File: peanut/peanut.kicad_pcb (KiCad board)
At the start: 4 copper layers, 48.2 x 24.5 mm, 75 parts, among them J1 USB-C, J2 PYRO_OUT, J3 Battery JST, J4 Arming, Q1 NMOS, Q2 NMOS, Q3 NMOS, Q4 NMOS, Q5 PMOS, U1 MS5611-01BA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

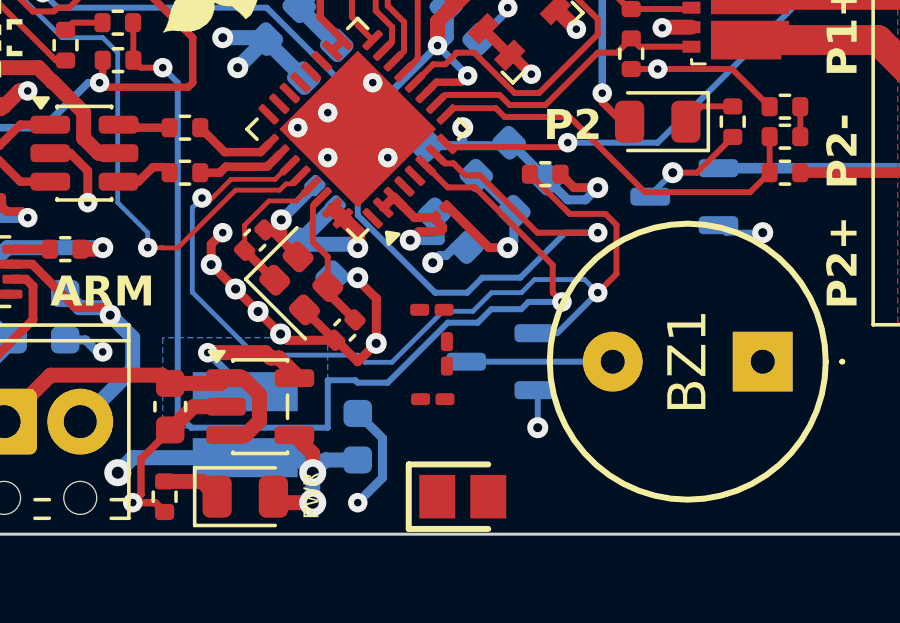
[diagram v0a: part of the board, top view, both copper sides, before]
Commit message: feat: Route the Bluetooth trace
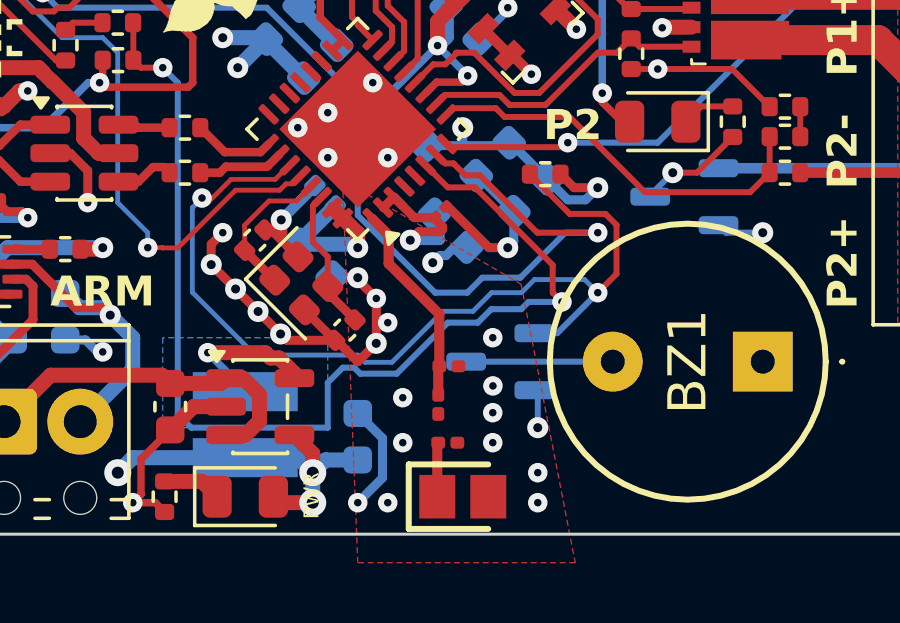
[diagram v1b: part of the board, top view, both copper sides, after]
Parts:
- C12, C13: footprint Capacitor_SMD:C_0201_0603Metric_Pad0.64x0.40mm_HandSolder -> Capacitor_SMD:C_0201_0603Metric
- L2: footprint Inductor_SMD:L_0201_0603Metric_Pad0.64x0.40mm_HandSolder -> Inductor_SMD:L_0201_0603Metric
- moved C12 1.97 mm to (146.0, 103.9), turned to 0 degrees
- moved L2 1.71 mm to (145.7, 105.2)
- moved C13 1.53 mm to (146.0, 106.4), turned to 0 degrees
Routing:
- net /RF_LNA_IN: track 0.00 -> 6.81 mm
- net /RF: track 0.00 -> 1.88 mm
- net GND: vias 38 -> 49
- added copper zone on F.Cu, net GND

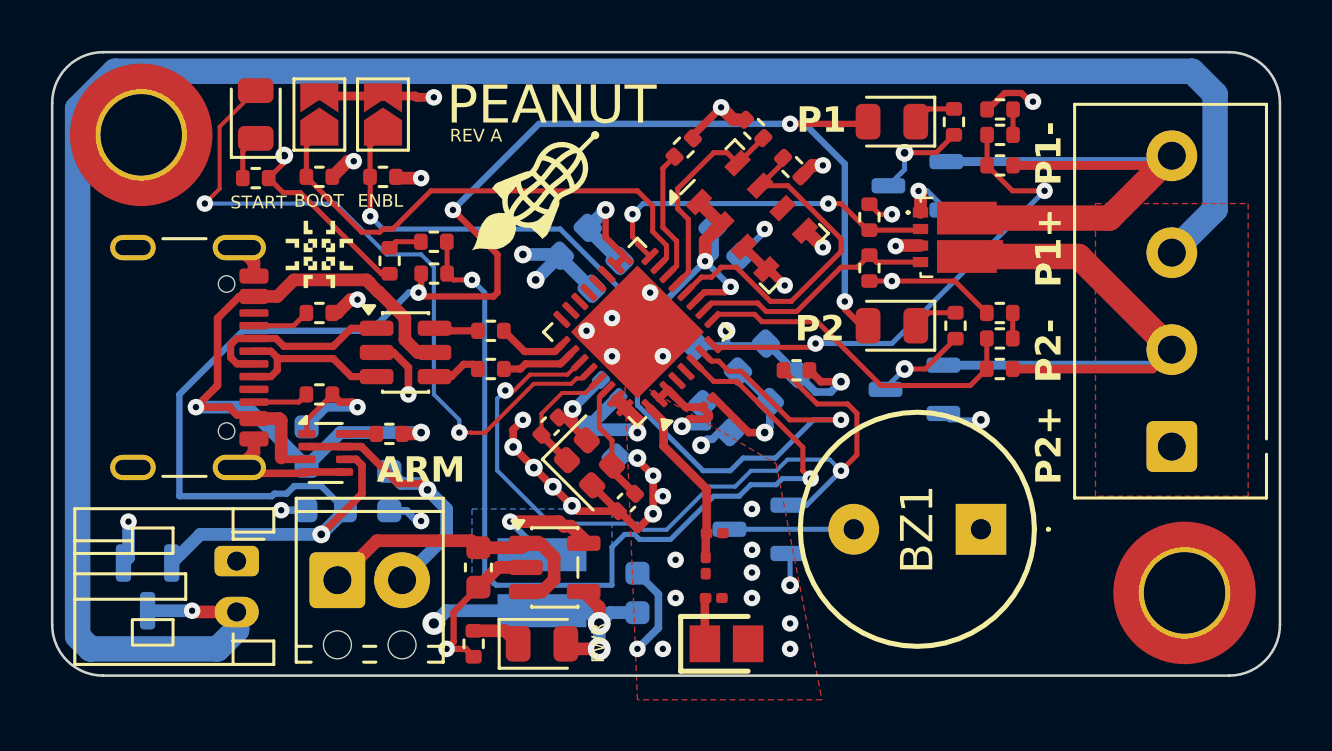
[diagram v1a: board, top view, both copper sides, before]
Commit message: bug: Fix arming flaw
Fixed the arming circuitry so that the ARM terminal prevents power going
to the pyro channels. This means that the rest of the board can be
powered on before arming, which is good because:

- It allows configuring without arming
- Software arming can still be done as a second stage
- The MCU can be in low-power mode until told to arm over BLE
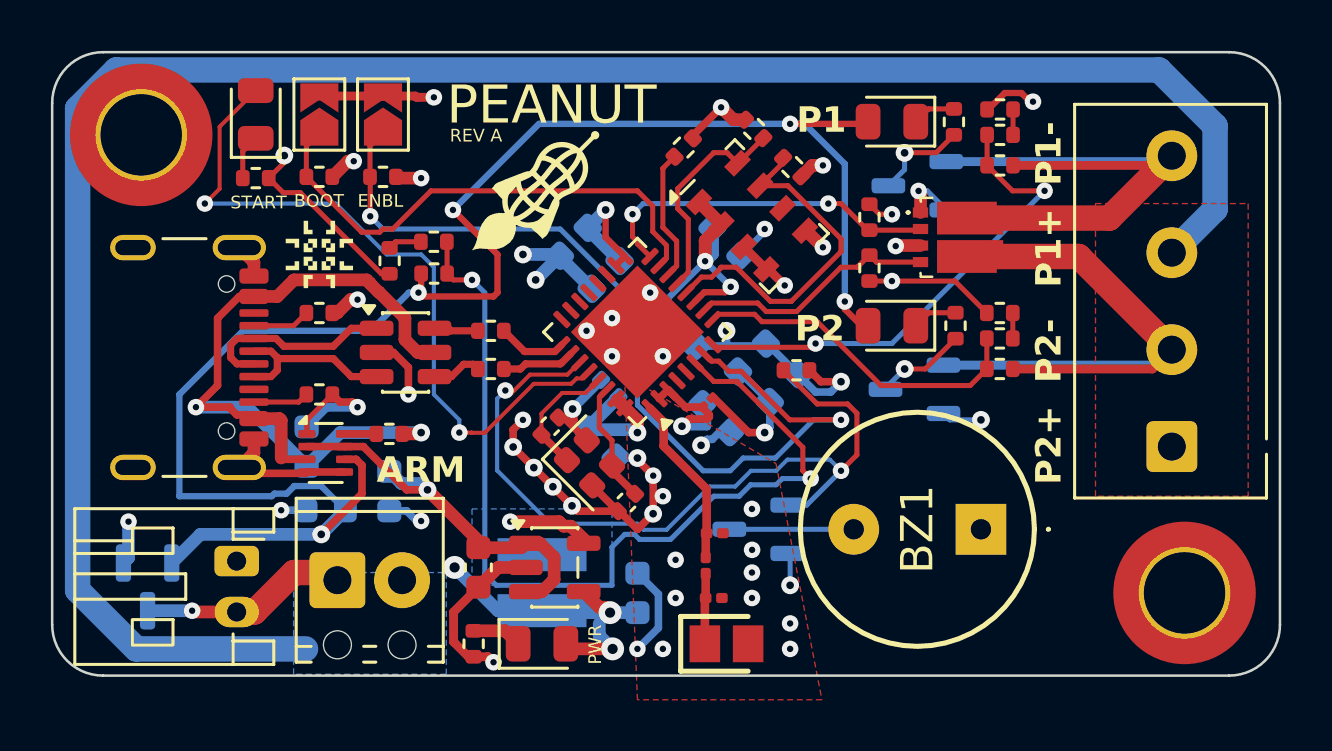
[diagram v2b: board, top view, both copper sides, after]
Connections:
- C18 pad 1: /Power/PWR_SRC -> /Power/REG_IN
- J2 pad 1: VBAT_RAW -> VPYRO
- J2 pad 3: VBAT_RAW -> VPYRO
- J4 pad 1: /Power/REG_IN -> VBAT_RAW
- J4 pad 2: /Power/PWR_SRC -> VPYRO
- U5 pad 2: /Power/PWR_SRC -> /Power/REG_IN
- U5 pad 7: /Power/PWR_SRC -> /Power/REG_IN
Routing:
- net VPYRO: track 0.00 -> 80.8 mm
- net VBAT_RAW: track 84.3 -> 8.25 mm
- net /Power/PWR_SRC: track 11.8 -> 0.00 mm, vias 1 -> 0
- net /Power/REG_IN: track 11.8 -> 15.8 mm, vias 0 -> 1
- net Net-(U4-SW): track 5.15 -> 3.39 mm
- net /RF: track 1.88 -> 2.84 mm
- added copper zone on B.Cu, net VPYRO
- added copper zone on F.Cu, net VPYRO
- removed copper zone on F.Cu, net VBAT_RAW

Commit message: chore: Clean up routing
Cleaned up some traces and added teardrops.
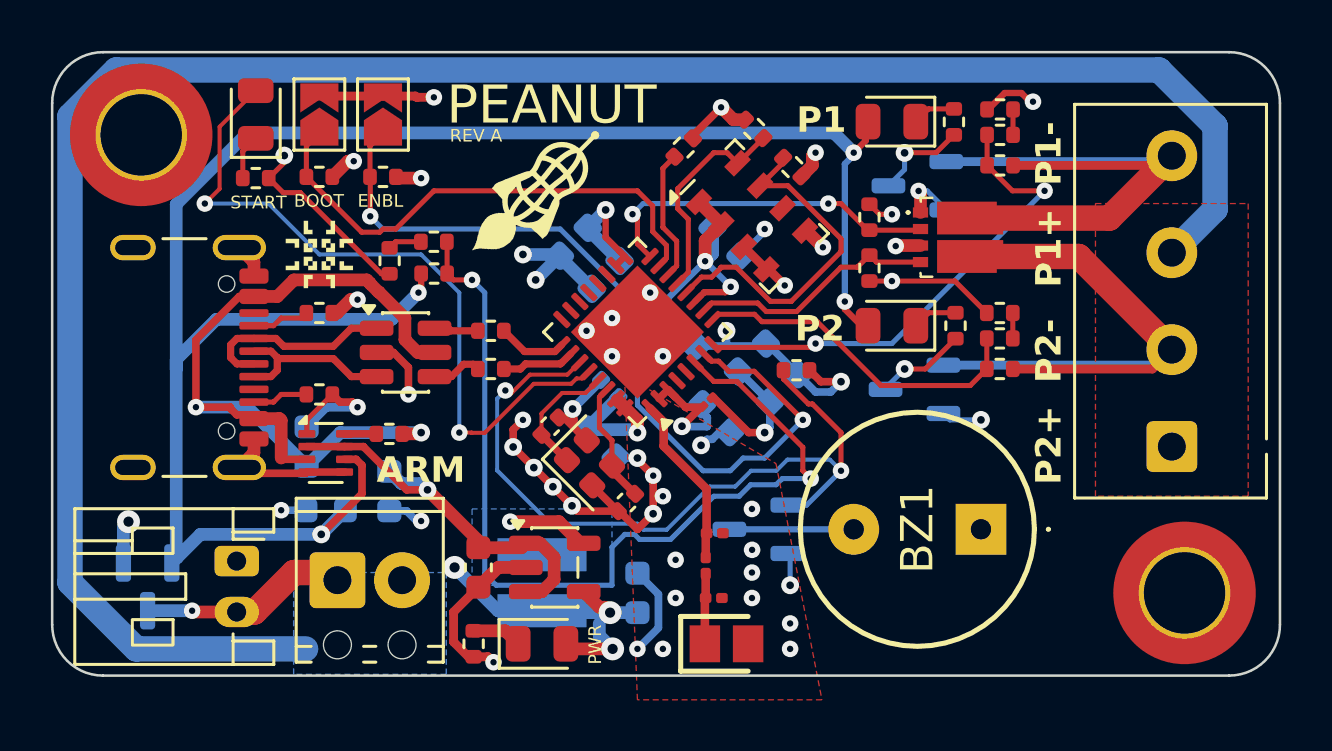
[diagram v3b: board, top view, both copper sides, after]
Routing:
- net VBAT: track 69.4 -> 74.6 mm, vias 5 -> 4
- net /ENABLE: track 35.7 -> 32.7 mm
- net /BUZ_PWM: track 31.4 -> 30.2 mm
- net /VDD3P3: track 6.22 -> 5.48 mm

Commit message: chore: More MCU ground vias
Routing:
- net GND: vias 49 -> 51

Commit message: chore: add dimensions
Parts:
- turned H1 to 180 degrees

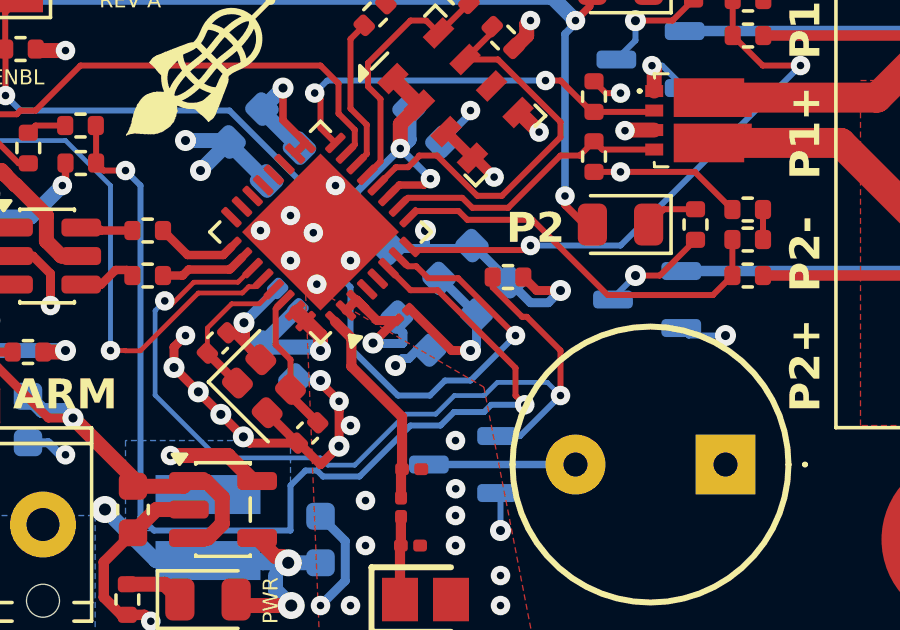
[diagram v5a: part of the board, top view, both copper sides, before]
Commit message: chore: fix inductor footprint size
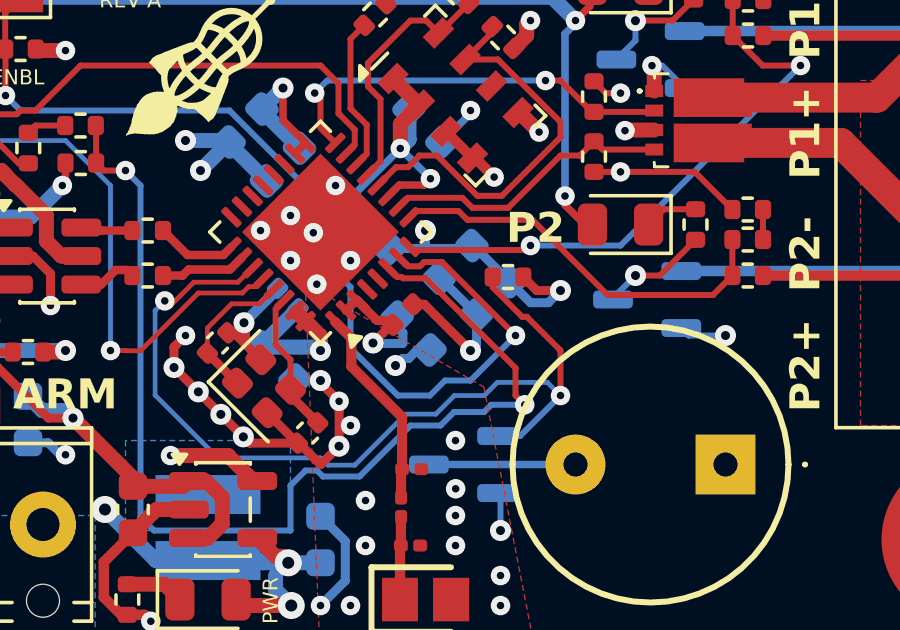
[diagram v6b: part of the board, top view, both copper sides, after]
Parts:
- removed REF**: OSHW-Logo_5.7x6mm_SilkScreen, Symbol:OSHW-Logo_5.7x6mm_SilkScreen
- L1: footprint Inductor_SMD:L_01005_0402Metric -> Inductor_SMD:L_0402_1005Metric

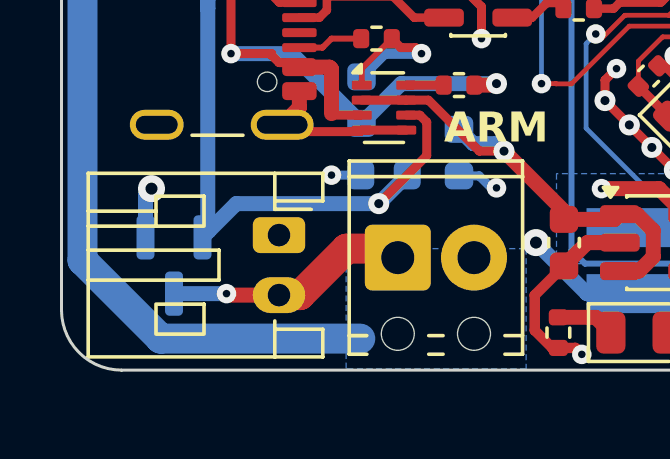
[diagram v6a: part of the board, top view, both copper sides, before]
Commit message: feat: Better arming circuit
Improved the arming circuit connections so that both circuits are
powered off until armed.

Signed-off-by: Matteo Golin <matteo.golin@gmail.com>
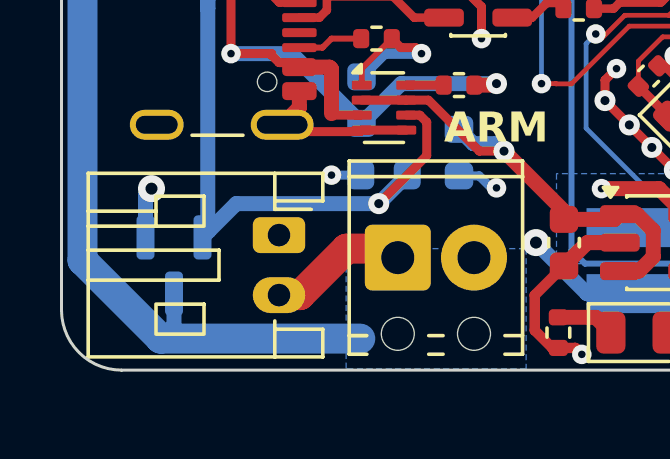
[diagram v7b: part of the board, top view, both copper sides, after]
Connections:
- J2 pad 1: VPYRO -> VBAT_CON
- J2 pad 3: VPYRO -> VBAT_CON
- J4 pad 2: VPYRO -> VBAT_CON
- Q5 pad 3: VBAT_RAW -> VBAT_CON
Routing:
- net VBAT_CON: track 0.00 -> 82.7 mm
- net VPYRO: track 81.0 -> 0.00 mm
- net VBAT_RAW: track 8.25 -> 4.73 mm, vias 1 -> 0
- added copper zone on B.Cu, net VBAT_CON
- added copper zone on F.Cu, net VBAT_CON
- removed copper zone on B.Cu, net VPYRO
- removed copper zone on F.Cu, net VPYRO

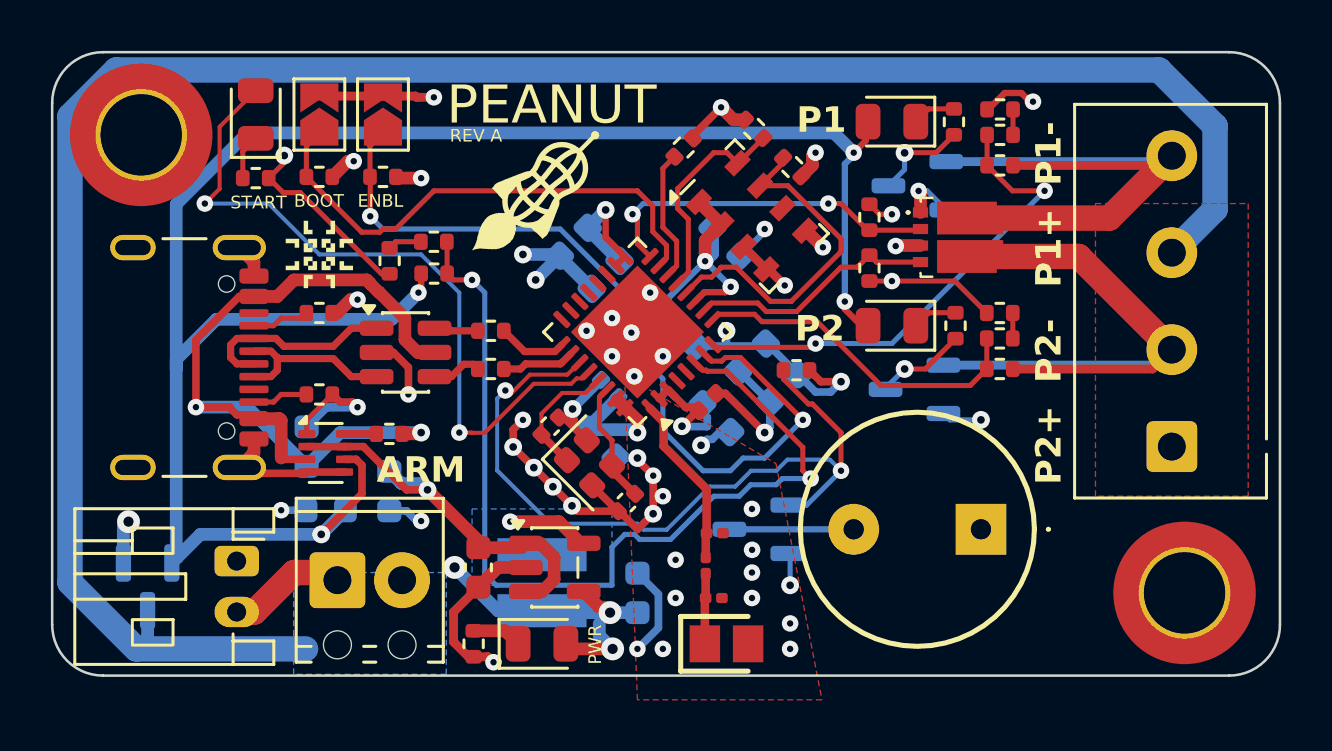
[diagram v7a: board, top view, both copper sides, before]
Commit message: feat: Move USB closer to the edge.
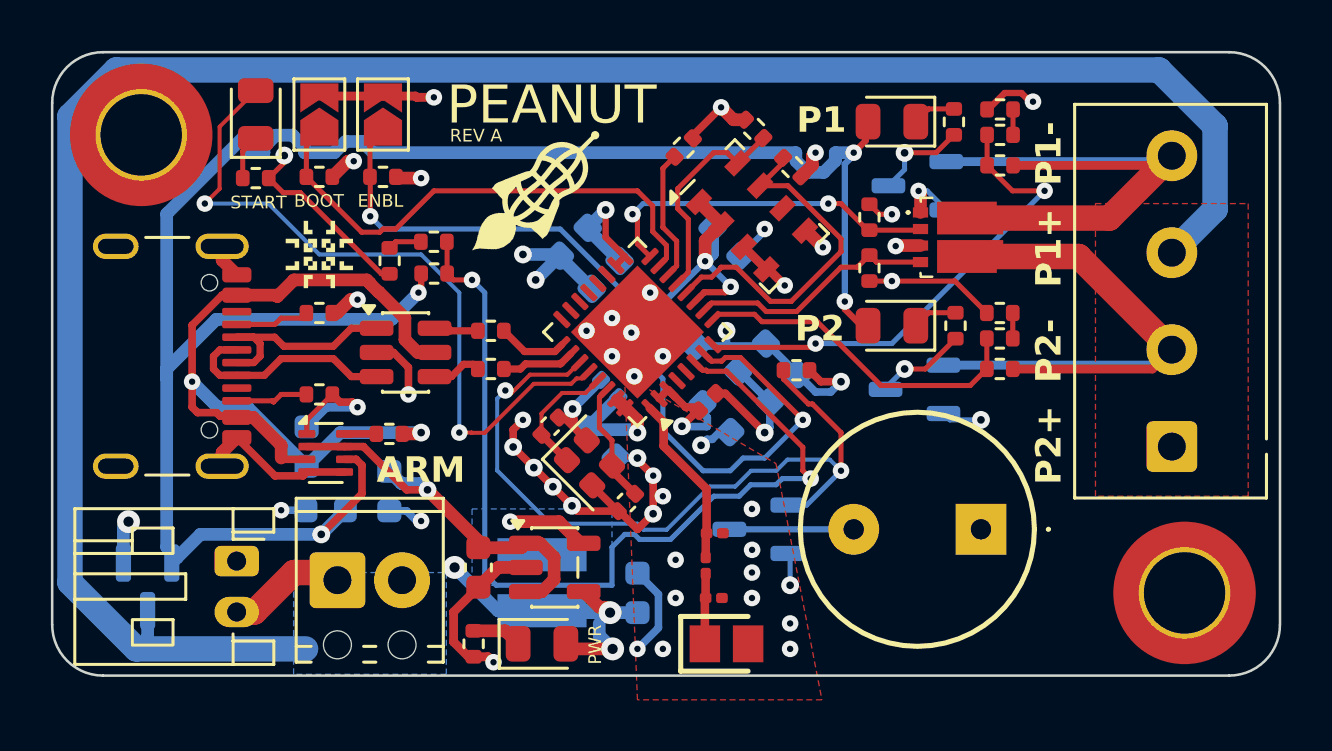
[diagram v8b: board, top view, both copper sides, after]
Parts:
- moved J1 0.68 mm to (123.6, 96.9)
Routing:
- net VBAT: track 74.6 -> 78.1 mm
- net /D+: track 6.75 -> 8.60 mm
- net Net-(J1-CC2): track 2.18 -> 2.88 mm
- net /D-: track 7.78 -> 8.48 mm
- net GND: track 93.1 -> 93.8 mm
- net Net-(J1-CC1): track 2.27 -> 2.92 mm
